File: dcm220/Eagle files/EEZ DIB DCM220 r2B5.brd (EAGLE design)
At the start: 155 x 95 mm, 248 parts, among them IC1 Si8662AB-B-IS1, IC10 MC33272ADR2G, IC11 LT3763EFE#PBF, IC12 MC33274ADR2G, IC13 LT3763EFE#PBF, IC2 TPS54060DGQ, IC3 Si8641AB-B-IS1, IC4 M24C32-WMN6P, IC5 LP2985-33DBVR, IC6 74HC2G04GW,125, IC7 N.C., IC8 STM32F373C8T6, IC9 TL431B, J1 4907, J2 571-0500, J3 571-0100, J4 571-0500, J5 571-0100, Q1 BSP716NH6327XTSA1, Q10 BSS84, Q2 NTD5867NLT4G, Q3 NTD5867NLT4G, Q4 BSS205NH6327XTSA1, Q5 BSS84, Q6 BSP716NH6327XTSA1, Q7 NTD5867NLT4G, Q8 NTD5867NLT4G, Q9 BSS205NH6327XTSA1, X1 39-30-1020, X2 77317-104-28LF, X3 N.C., X4 DS1024-2*5R0, Y1 LF XTAL026392

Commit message: DCM220 r2B5
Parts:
- removed SH1, SH3, SH4: (no value), EEZ_Lib1:SHORT_NOHOLE
- R30, R32, R54, R56: value 22K -> 20K
- R31, R33, R55, R57: value 10K -> 12K
- moved FB1 18.4 mm to (113.3, 33.5), turned to 90 degrees
- moved IC9 16.0 mm to (118.4, 33.2)
- moved C38 12.3 mm to (114.5, 36.8), turned to 180 degrees
- moved C37 10.9 mm to (114.5, 38.7), turned to 180 degrees
- moved R23 8.55 mm to (115.3, 32.9), turned to 90 degrees
- moved R19 6.22 mm to (116.2, 18.9), turned to 180 degrees
- moved C44 4.99 mm to (110.5, 34.2), turned to 0 degrees
- moved R27 3.27 mm to (110.5, 36.2), turned to 180 degrees
- moved C28 2.29 mm to (127.5, 46.8)
- moved C29 2.29 mm to (127.0, 48.8)
- moved C39 2.29 mm to (118.4, 36.7)
- moved C40 2.29 mm to (113.6, 46.3)
- moved C41 2.29 mm to (110.5, 46.0)
- moved C43 2.29 mm to (110.5, 38.2)
- moved IC8 2.29 mm to (120.3, 43.3)
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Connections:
- removed net DC_OUT-: C2.1, C46.-, C50.2, C52.2, C57.2, C59.2, C60.2, C61.2, C62.-, C63.2, C68.-, C71.2, C72.2, C77.2, C79.2, C80.2, C81.2, C82.-, C83.2, CH1.GND, CH2.GND, D12.A, D7.A, J3.1, J3.1.1, J5.1, J5.1.1, L1.2, LED1.CC, LED2.CC, Q3.3, Q8.3, R37.1, R41.2, R61.1, R65.2, SH1.2, SH3.1, SH4.1, X4.1, X4.10, X4.2, X4.3, X4.4, X4.5, X4.6, X4.7, X4.8, X4.9, ZD1.A, ZD3.A, ZD5.A
- net +VREF: now also IC8.9
- net AGND: now also IC9.3
- net GND: now also C2.1, C46.-, C50.2, C52.2, C57.2, C59.2, C60.2, C61.2, C62.-, C63.2, C68.-, C71.2, C72.2, C77.2, C79.2, C80.2, C81.2, C82.-, C83.2, CH1.GND, CH2.GND, D12.A, D7.A, J3.1, J3.1.1, J5.1, J5.1.1, L1.2, LED1.CC, LED2.CC, Q3.3, Q8.3, R37.1, R41.2, R61.1, R65.2, X4.1, X4.10, X4.2, X4.3, X4.4, X4.5, X4.6, X4.7, X4.8, X4.9, ZD1.A, ZD3.A, ZD5.A; no longer IC9.3, SH1.1, SH3.2, SH4.2
- net VDDA: no longer IC8.9
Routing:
- net DC_OUT-: track 223.7 -> 0.00 mm, vias 26 -> 0
- net GND: track 113.2 -> 301.7 mm, vias 110 -> 146
- net VDDA: track 20.7 -> 8.30 mm, vias 2 -> 0
- net +3V3: track 431.5 -> 439.3 mm
- net I_MON2: track 43.9 -> 39.5 mm
- net TEMP#2: track 43.3 -> 46.6 mm
- net TEMP#1: track 64.5 -> 61.2 mm
- net OE#2: track 155.0 -> 158.0 mm
- net I_MON#2: track 7.59 -> 10.3 mm
- net CC_LED#1: track 121.5 -> 118.8 mm
- net NRST: track 21.9 -> 24.6 mm
- net CC_LED#2: track 115.4 -> 117.6 mm
- net BOOT0: track 54.6 -> 56.9 mm
- net SCLK: track 38.3 -> 40.6 mm
- net U_SET_OUT#1: track 23.3 -> 21.0 mm
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- removed copper zone on layer 1, net DC_OUT-
- removed copper zone on layer 16, net DC_OUT-
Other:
- board text added: "EEZ DIB DCM220 (10/2019 r2B5)"
- board text added: "EEZ DIB DCM220 (10/2019 r2B5) Project source code: github.com/eez-open"
- board text removed: "EEZ DIB DCM220 (10/2019 r2B4)"
- board text removed: "EEZ DIB DCM220 (10/2019 r2B4) Project source code: github.com/eez-open"

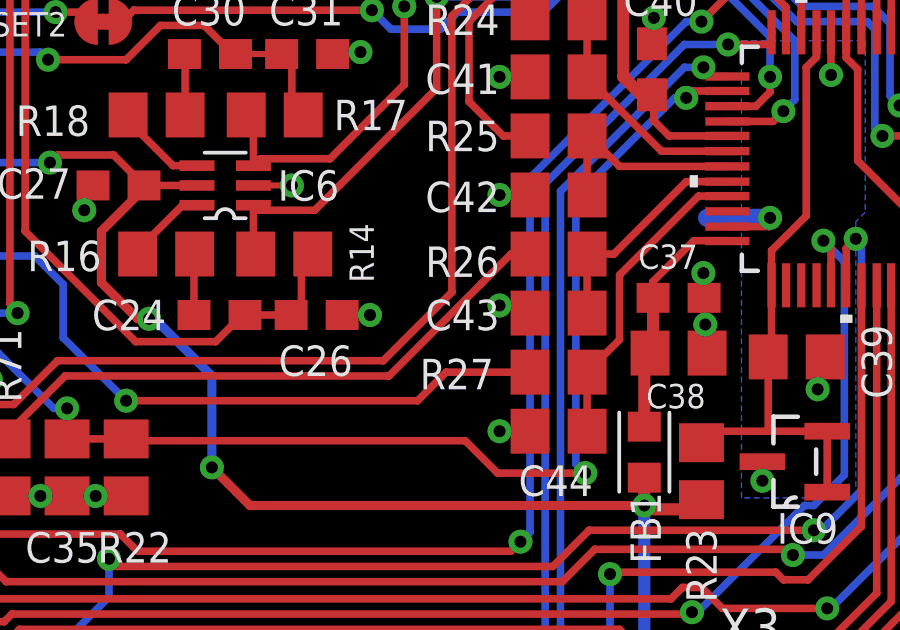
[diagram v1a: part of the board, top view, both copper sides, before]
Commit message: DCM220 modified U_SET dividers
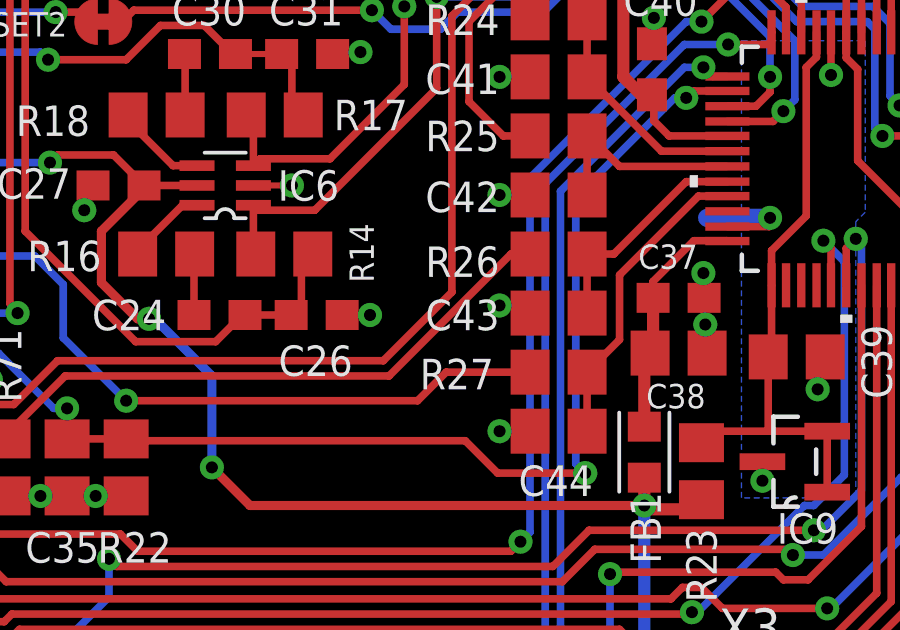
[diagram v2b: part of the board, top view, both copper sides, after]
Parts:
- R46, R70: value 3K9 -> 3K6
- R48, R72: value 3K6 -> 3K3
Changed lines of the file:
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@@
 <layer number="20" name="Dimension" color="4" fill="1" visible="yes" active="yes"/>
 <layer number="21" name="tPlace" color="7" fill="1" visible="yes" active="yes"/>
-<layer number="22" name="bPlace" color="6" fill="1" visible="yes" active="yes"/>
-<layer number="23" name="tOrigins" color="15" fill="1" visible="yes" active="yes"/>
+<layer number="22" name="bPlace" color="6" fill="1" visible="no" active="yes"/>
+<layer number="23" name="tOrigins" color="15" fill="1" visible="no" active="yes"/>
 <layer number="24" name="bOrigins" color="15" fill="1" visible="no" active="yes"/>
 <layer number="25" name="tNames" color="7" fill="1" visible="yes" active="yes"/>
@@
 <attribute name="VALUE" x="85.725" y="70.993" size="1.016" layer="27" ratio="10" rot="R90"/>
 </element>
-<element name="R46" library="rcl" package="R0805" value="3K9" x="83.2485" y="72.263" smashed="yes" rot="R90">
+<element name="R46" library="rcl" package="R0805" value="3K6" x="83.2485" y="72.263" smashed="yes" rot="R90">
 <attribute name="NAME" x="82.7405" y="70.1675" size="1.016" layer="25" ratio="10" rot="R270"/>
 <attribute name="VALUE" x="83.7565" y="70.993" size="1.016" layer="27" ratio="10" rot="R90"/>
 </element>
-<element name="R48" library="rcl" package="R0805" value="3K6" x="87.1855" y="72.263" smashed="yes" rot="R90">
+<element name="R48" library="rcl" package="R0805" value="3K3" x="87.1855" y="72.263" smashed="yes" rot="R90">
 <attribute name="NAME" x="86.741" y="70.1675" size="1.016" layer="25" ratio="10" rot="R270"/>
 <attribute name="VALUE" x="87.63" y="70.866" size="1.016" layer="27" ratio="10" rot="R90"/>
@@
 <attribute name="VALUE" x="84.7725" y="34.6075" size="1.016" layer="27" ratio="10" rot="R270"/>
 </element>
-<element name="R70" library="rcl" package="R0805" value="3K9" x="83.3755" y="33.02" smashed="yes" rot="R90">
+<element name="R70" library="rcl" package="R0805" value="3K6" x="83.3755" y="33.02" smashed="yes" rot="R90">
 <attribute name="NAME" x="82.8675" y="31.0515" size="1.016" layer="25" ratio="10" rot="R270"/>
 <attribute name="VALUE" x="83.8835" y="31.6865" size="1.016" layer="27" ratio="10" rot="R90"/>
 </element>
-<element name="R72" library="rcl" package="R0805" value="3K6" x="87.3125" y="33.02" smashed="yes" rot="R270">
+<element name="R72" library="rcl" package="R0805" value="3K3" x="87.3125" y="33.02" smashed="yes" rot="R270">
 <attribute name="NAME" x="86.868" y="31.0515" size="1.016" layer="25" ratio="10" rot="R270"/>
 <attribute name="VALUE" x="86.8045" y="34.6075" size="1.016" layer="27" ratio="10" rot="R270"/>
@@
 <element name="R21" library="rcl" package="R0805" value="3K3" x="95.0595" y="72.263" smashed="yes" rot="R90">
 <attribute name="NAME" x="94.615" y="70.1675" size="1.016" layer="25" ratio="10" rot="R270"/>
-<attribute name="VALUE" x="95.6945" y="70.612" size="1.27" layer="27" rot="R90"/>
+<attribute name="VALUE" x="95.5675" y="70.9295" size="1.016" layer="27" ratio="10" rot="R90"/>
 </element>
 <element name="C34" library="rcl" package="C0805" value="10n" x="93.091" y="72.263" smashed="yes" rot="R270">
@@
 <element name="R22" library="rcl" package="R0805" value="3K3" x="96.0755" y="33.02" smashed="yes" rot="R270">
 <attribute name="NAME" x="95.123" y="29.845" size="1.016" layer="25" ratio="10"/>
-<attribute name="VALUE" x="96.7105" y="31.369" size="1.27" layer="27" rot="R90"/>
+<attribute name="VALUE" x="96.5835" y="31.6865" size="1.016" layer="27" ratio="10" rot="R90"/>
 </element>
 <element name="C35" library="rcl" package="C0805" value="10n" x="94.107" y="33.02" smashed="yes" rot="R90">
@@
 <wire x1="92.1385" y1="34.163" x2="94.0435" y2="36.068" width="0.254" layer="1"/>
 <wire x1="94.0435" y1="36.068" x2="104.8385" y2="36.068" width="0.254" layer="1"/>
-<wire x1="104.8385" y1="36.068" x2="107.91825" y2="39.14775" width="0.254" layer="1"/>
-<wire x1="107.91825" y1="39.14775" x2="108.2675" y2="39.497" width="0.254" layer="1"/>
 <wire x1="109.54" y1="40.132" x2="108.9025" y2="40.132" width="0.254" layer="1"/>
-<wire x1="108.9025" y1="40.132" x2="108.2675" y2="39.497" width="0.254" layer="1"/>
+<wire x1="104.8385" y1="36.068" x2="108.9025" y2="40.132" width="0.254" layer="1"/>
 </signal>
 <signal name="BOOT0">

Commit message: DCM220 PCB corrections
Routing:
- net +3V3: track 439.3 -> 433.0 mm, vias 19 -> 18
- net ISET1: track 23.1 -> 21.0 mm
- net U_SET#1: track 34.1 -> 36.0 mm
- net N$247: track 28.1 -> 29.1 mm
- net INTVCC2: track 30.2 -> 31.0 mm
- net N$39: track 42.7 -> 43.2 mm
- net DC_OUT+: track 296.8 -> 296.3 mm
- net ISET2: track 32.5 -> 32.2 mm, vias 2 -> 0
- net GND: track 301.7 -> 301.8 mm, vias 146 -> 154
